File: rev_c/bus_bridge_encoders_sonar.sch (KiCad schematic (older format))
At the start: 52 parts, among them J1 POWER_SELECT, J2 TERMINATE_JUMPER, SW1 MJTP1243, U1 LM2940, U2 LTV-826, U3 LTV-826, U4 LTV-826, U5 754410, U6 LM2940, U7 74HCT08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

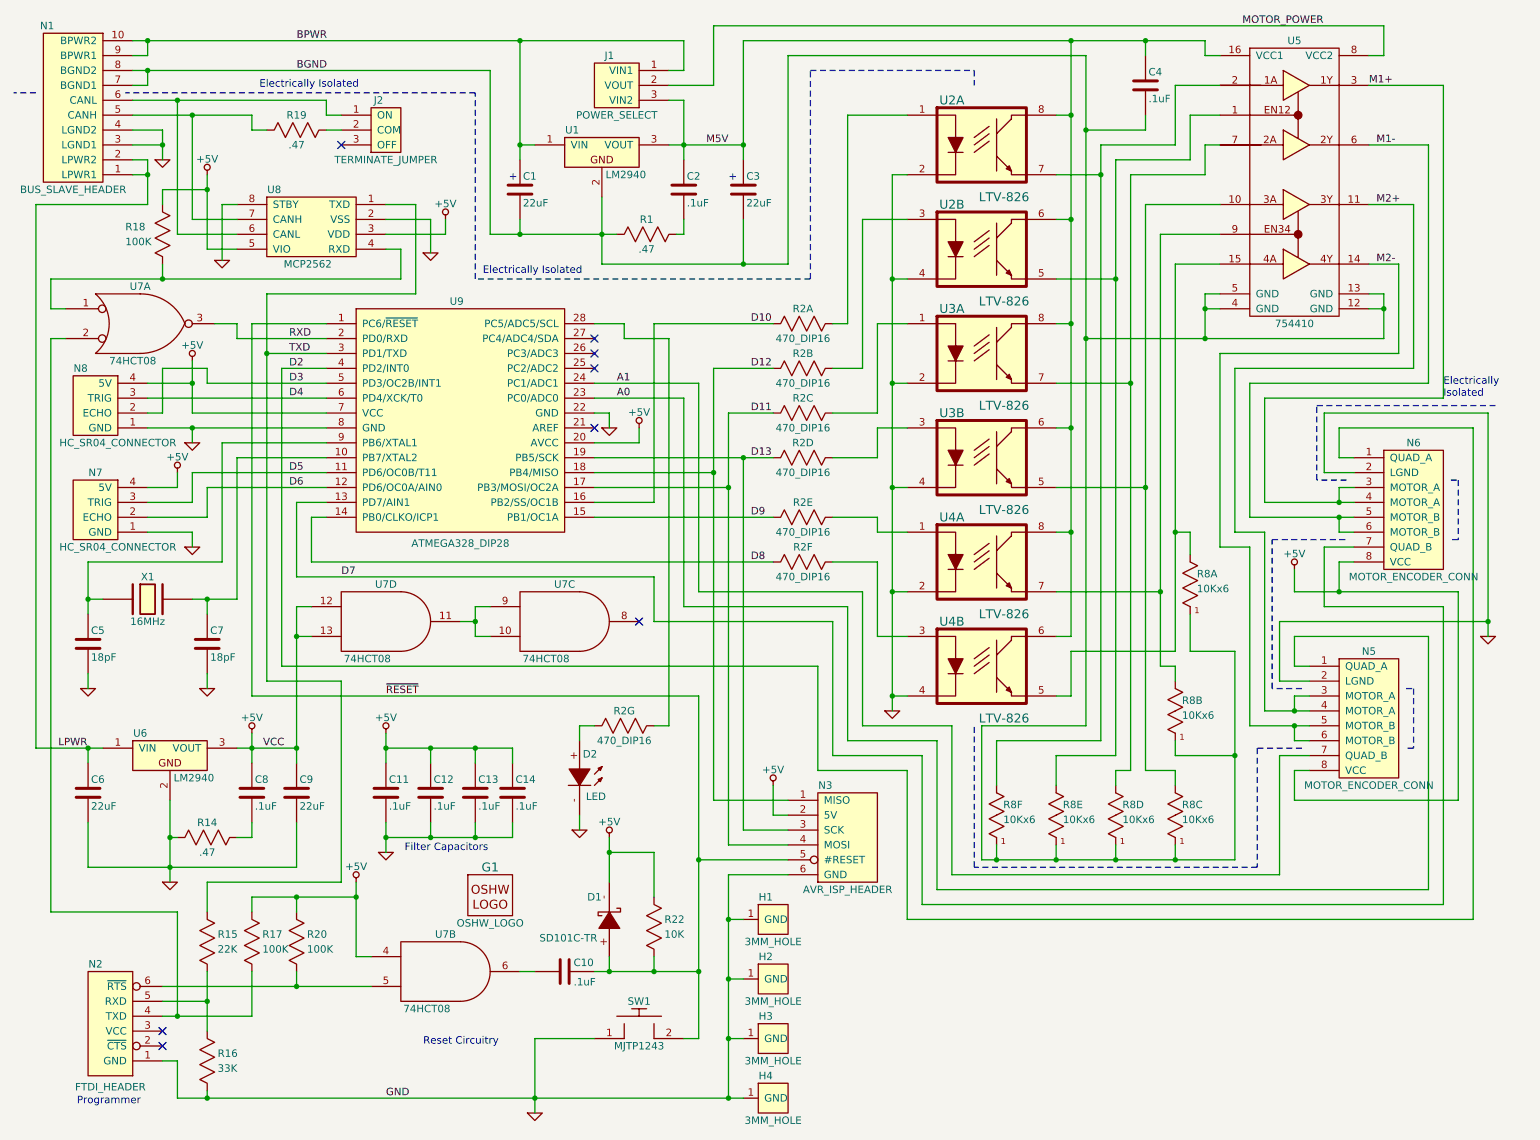
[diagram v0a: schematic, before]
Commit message: Forgot to commit Rev. C.  Also changed vertical resistors to from pin_header to Resistor_Vertical__100 footprint.
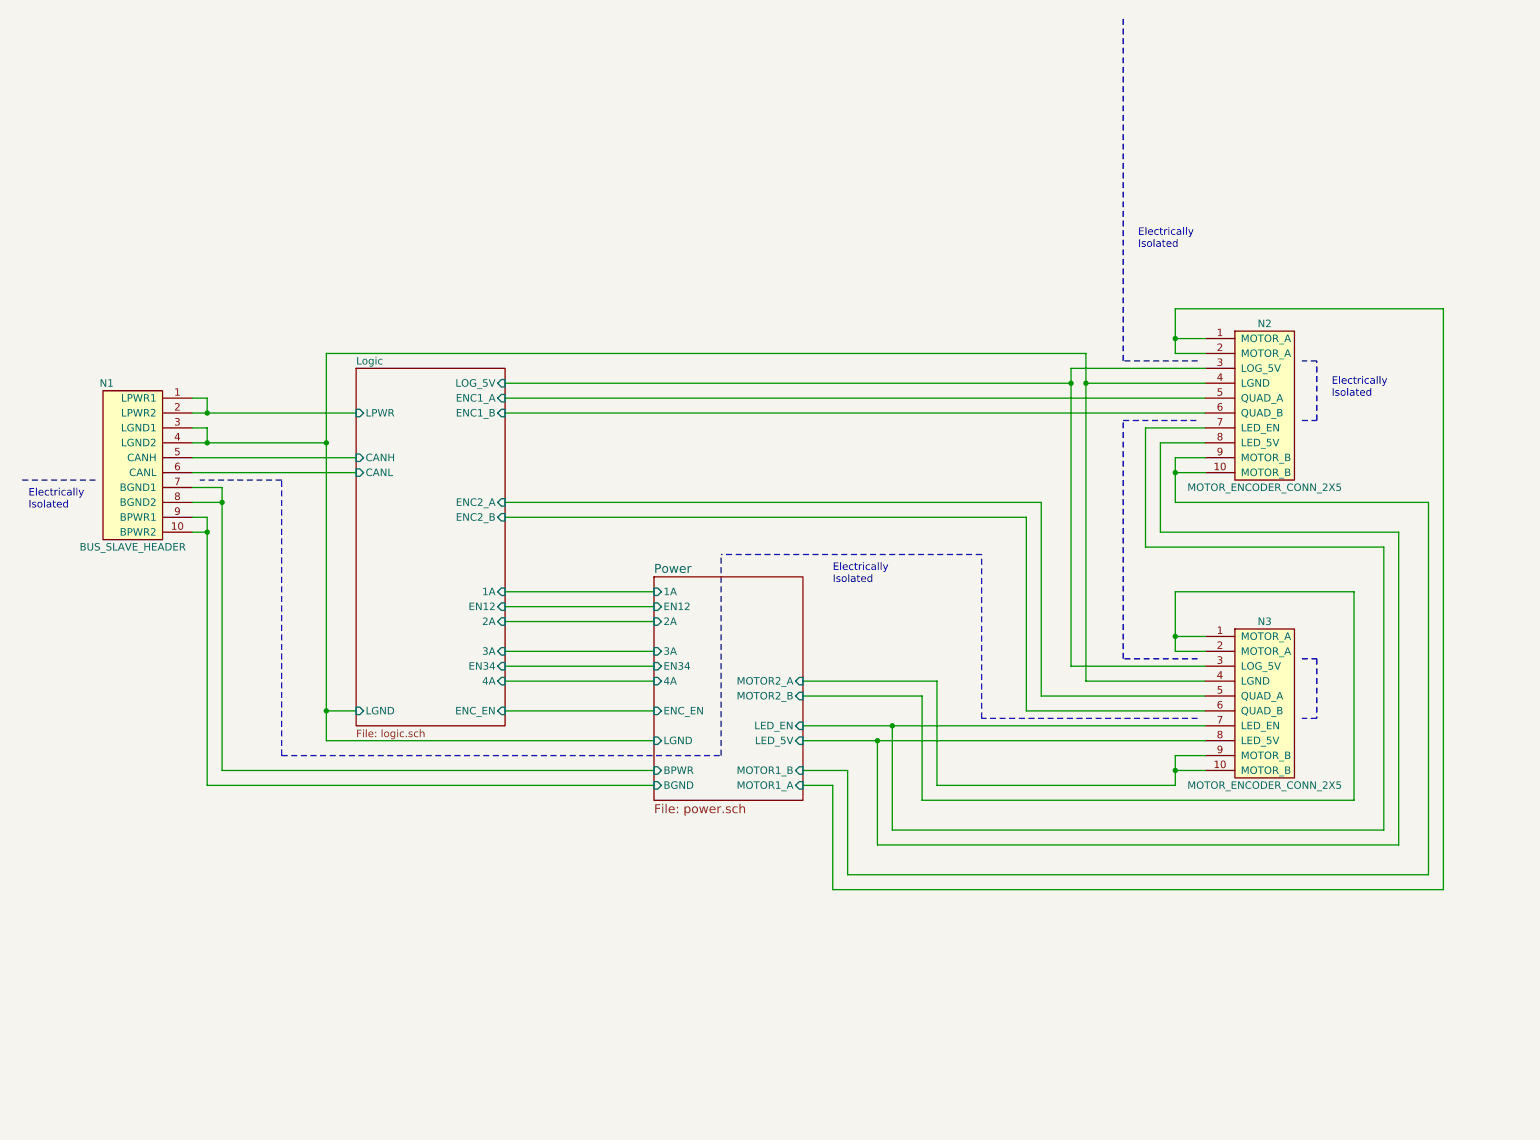
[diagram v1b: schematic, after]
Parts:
- removed C1, C3, C6, C9: 22uF, Bus_Bridge_Encoders_Sonar:Capacitor4x3RM2-5_RevB, symbol C_VERT
- removed C10: .1uF, Bus_Bridge_Encoders_Sonar:Capacitor3MMDiscRM2.5, symbol C_HORIZ
- removed C11, C12, C13, C14, C2, C4, C8: .1uF, Bus_Bridge_Encoders_Sonar:Capacitor3MMDiscRM2.5, symbol C_VERT
- removed C5, C7: 18pF, Bus_Bridge_Encoders_Sonar:Capacitor3MMDiscRM2.5, symbol C_VERT
- removed D1: SD101C-TR, Bus_Bridge_Encoders_Sonar:Diode_DO-41_SOD81_Horizontal_RM10, symbol SCHOTTKY_DIODE_VERT
- removed D2: LED, Bus_Bridge_Encoders_Sonar:T1_LED, symbol LED
- removed G1: OSHW_LOGO, Bus_Bridge_Encoders_Sonar:OSHW_LOGO_300mil, symbol OSHW_LOGO
- removed H1, H2, H3, H4: 3MM_HOLE, Bus_Bridge_Encoders_Sonar:MountingHole_3mm, symbol 3MM_HOLE
- removed J1: POWER_SELECT, Bus_Bridge_Encoders_Sonar:Pin_Header_Straight_1x03, symbol POWER_SELECT
- removed J2: TERMINATE_JUMPER, Bus_Bridge_Encoders_Sonar:Pin_Header_Straight_1x03, symbol TERMINATE_JUMPER
- removed N2: FTDI_HEADER, Bus_Bridge_Encoders_Sonar:Pin_Header_Straight_1x06, symbol FTDI_HEADER
- removed N3: AVR_ISP_HEADER, Bus_Bridge_Encoders_Sonar:Pin_Header_Straight_2x03, symbol AVR_ISP_HEADER
- removed N5, N6: MOTOR_ENCODER_CONN, Bus_Bridge_Encoders_Sonar:Pin_Header_Straight_2x04_Shrouded, symbol MOTOR_ENCODER_CONN
- removed N7, N8: HC_SR04_CONNECTOR, Bus_Bridge_Encoders_Sonar:Pin_Header_Straight_1x04, symbol HC_SR04_CONNECTOR
- removed R1, R14, R19: .47, Bus_Bridge_Encoders_Sonar:Resistor_Horizontal_400, symbol R_HORIZ
- removed R15: 22K, Bus_Bridge_Encoders_Sonar:Resistor_Horizontal_400, symbol R_VERT
- removed R16: 33K, Bus_Bridge_Encoders_Sonar:Resistor_Horizontal_400, symbol R_VERT
- removed R17, R18, R20: 100K, Bus_Bridge_Encoders_Sonar:Resistor_Horizontal_400, symbol R_VERT
- removed R2: 470_DIP16, Bus_Bridge_Encoders_Sonar:DIP-16__300, symbol R_HORIZ_DIP16
- removed R22: 10K, Bus_Bridge_Encoders_Sonar:Resistor_Horizontal_400, symbol R_VERT
- removed R8: 10Kx6, Bus_Bridge_Encoders_Sonar:Pin_Header_Straight_1x07, symbol R_VERT_SIP7
- removed SW1: MJTP1243, Bus_Bridge_Encoders_Sonar:Button_6.5MM, symbol 2_LEAD_PUSH_BUTTON
- removed U1, U6: LM2940, Bus_Bridge_Encoders_Sonar:TO-220_Neutral123_Horizontal_LargePads, symbol VOLTAGE_REGULATOR
- removed U2, U3, U4: LTV-826, Bus_Bridge_Encoders_Sonar:DIP-8__300, symbol OPTO_ISOLATOR
- removed U5: 754410, Bus_Bridge_Encoders_Sonar:DIP-16__300, symbol 754410
- removed U7: 74HCT08, Bus_Bridge_Encoders_Sonar:DIP-14__300, symbol 74X08
- removed U8: MCP2562, Bus_Bridge_Encoders_Sonar:DIP-8__300, symbol MCP2562
- removed U9: ATMEGA328_DIP28, Bus_Bridge_Encoders_Sonar:DIP-28__300, symbol ATMEGA328_DIP28
- removed X1: 16MHz, Bus_Bridge_Encoders_Sonar:Crystal_HC49-U_Vertical, symbol CRYSTAL
- added N2, N3: MOTOR_ENCODER_CONN_2X5, Bus_Bridge_Encoders_Sonar:Pin_Header_Straight_2x05_Shrouded, symbol MOTOR_ENCODER_CONN_2X5
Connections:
- net Logic/CANH: now reaches N1.5 (CANH)
- net Logic/CANL: now reaches N1.6 (CANL)
- net BGND renamed Power/BPWR
- net BPWR renamed Power/BGND
- net GND renamed Logic/LGND
- net Logic/LGND: now also N2.4 (LGND), N3.4 (LGND)
- net LPWR renamed Logic/LPWR
- new net Logic/ENC1_A: N2.5 (QUAD_A)
- new net Logic/ENC1_B: N2.6 (QUAD_B)
- new net Logic/ENC2_A: N3.5 (QUAD_A)
- new net Logic/ENC2_B: N3.6 (QUAD_B)
- new net Logic/LOG_5V: N2.3 (LOG_5V), N3.3 (LOG_5V)
- new net Power/LED_5V: N2.8 (LED_5V), N3.8 (LED_5V)
- new net Power/LED_EN: N2.7 (LED_EN), N3.7 (LED_EN)
- new net Power/MOTOR1_A: N2.1 (MOTOR_A), N2.2 (MOTOR_A)
- new net Power/MOTOR1_B: N2.10 (MOTOR_B), N2.9 (MOTOR_B)
- new net Power/MOTOR2_A: N3.10 (MOTOR_B), N3.9 (MOTOR_B)
- new net Power/MOTOR2_B: N3.1 (MOTOR_A), N3.2 (MOTOR_A)
- no-connect marks 8 -> 0
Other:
- note removed: "+"
- note removed: "Electrically Isolated"
- note removed: "Filter Capacitors"
- note removed: "Programmer"
- note removed: "Reset Circuitry"
